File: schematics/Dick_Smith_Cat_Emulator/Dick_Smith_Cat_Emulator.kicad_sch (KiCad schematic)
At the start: 9 parts, among them J1 Expansion Connector

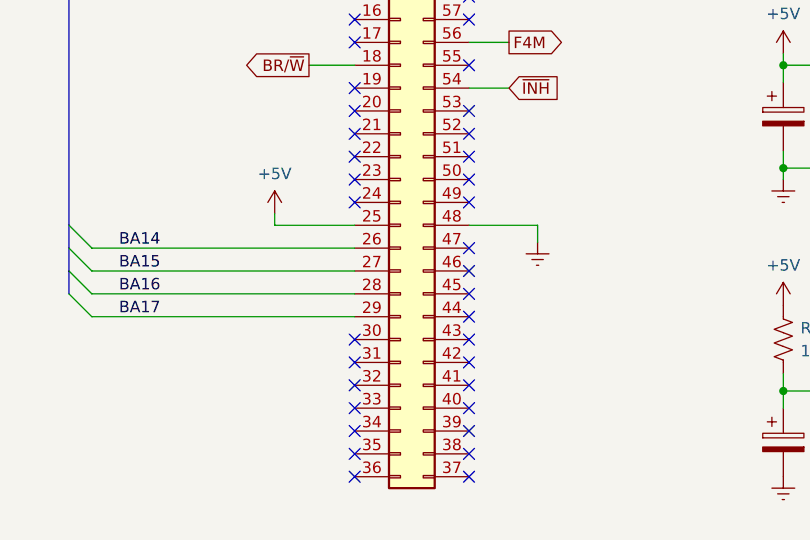
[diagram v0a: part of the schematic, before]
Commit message: Update emulator schematic upon inspection of board
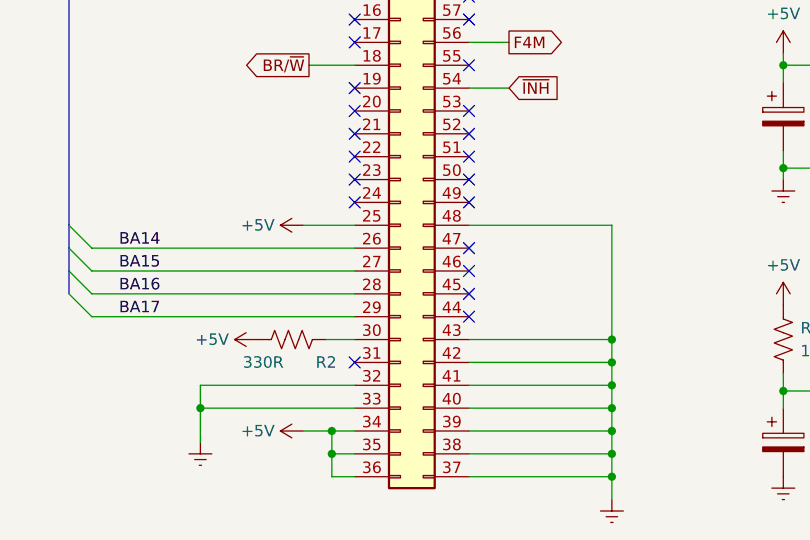
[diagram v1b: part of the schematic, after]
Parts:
- added R2: 330R, symbol Device:R_US
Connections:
- net +5V: now also J1.34 (Pin_34), J1.35 (Pin_35), J1.36 (Pin_36), R2.1
- net Earth: now also J1.32 (Pin_32), J1.33 (Pin_33), J1.37 (Pin_37), J1.38 (Pin_38), J1.39 (Pin_39), J1.40 (Pin_40), J1.41 (Pin_41), J1.42 (Pin_42), J1.43 (Pin_43)
- net at J1.30 (Pin_30): now also R2.2
- no-connect marks 38 -> 25
